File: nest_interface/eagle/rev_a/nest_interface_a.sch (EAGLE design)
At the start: 98 parts, among them J1 MOLEX_MICRO_USB_B_047346, J10 CONN_BLOCK_2, J11 CONN_BLOCK_2, J12 CONN_BLOCK_2, J13 CONN_BLOCK_2, J14 CONN_BLOCK_2, J15 CONN_BLOCK_2, J16 CONN_BLOCK_2, J17 CONN_BLOCK_3, J2 CONN_BLOCK_2, J3 CONN_BLOCK_3, J4 PJ-036A-SMT, J5 CONN_BLOCK_3, J6 CONN_BLOCK_3, J7 CONN_BLOCK_2, J8 CONN_BLOCK_3, J9 CONN_BLOCK_3, U1 FT232RL, U2 EPIC-CORE_A, U3 MPC1825

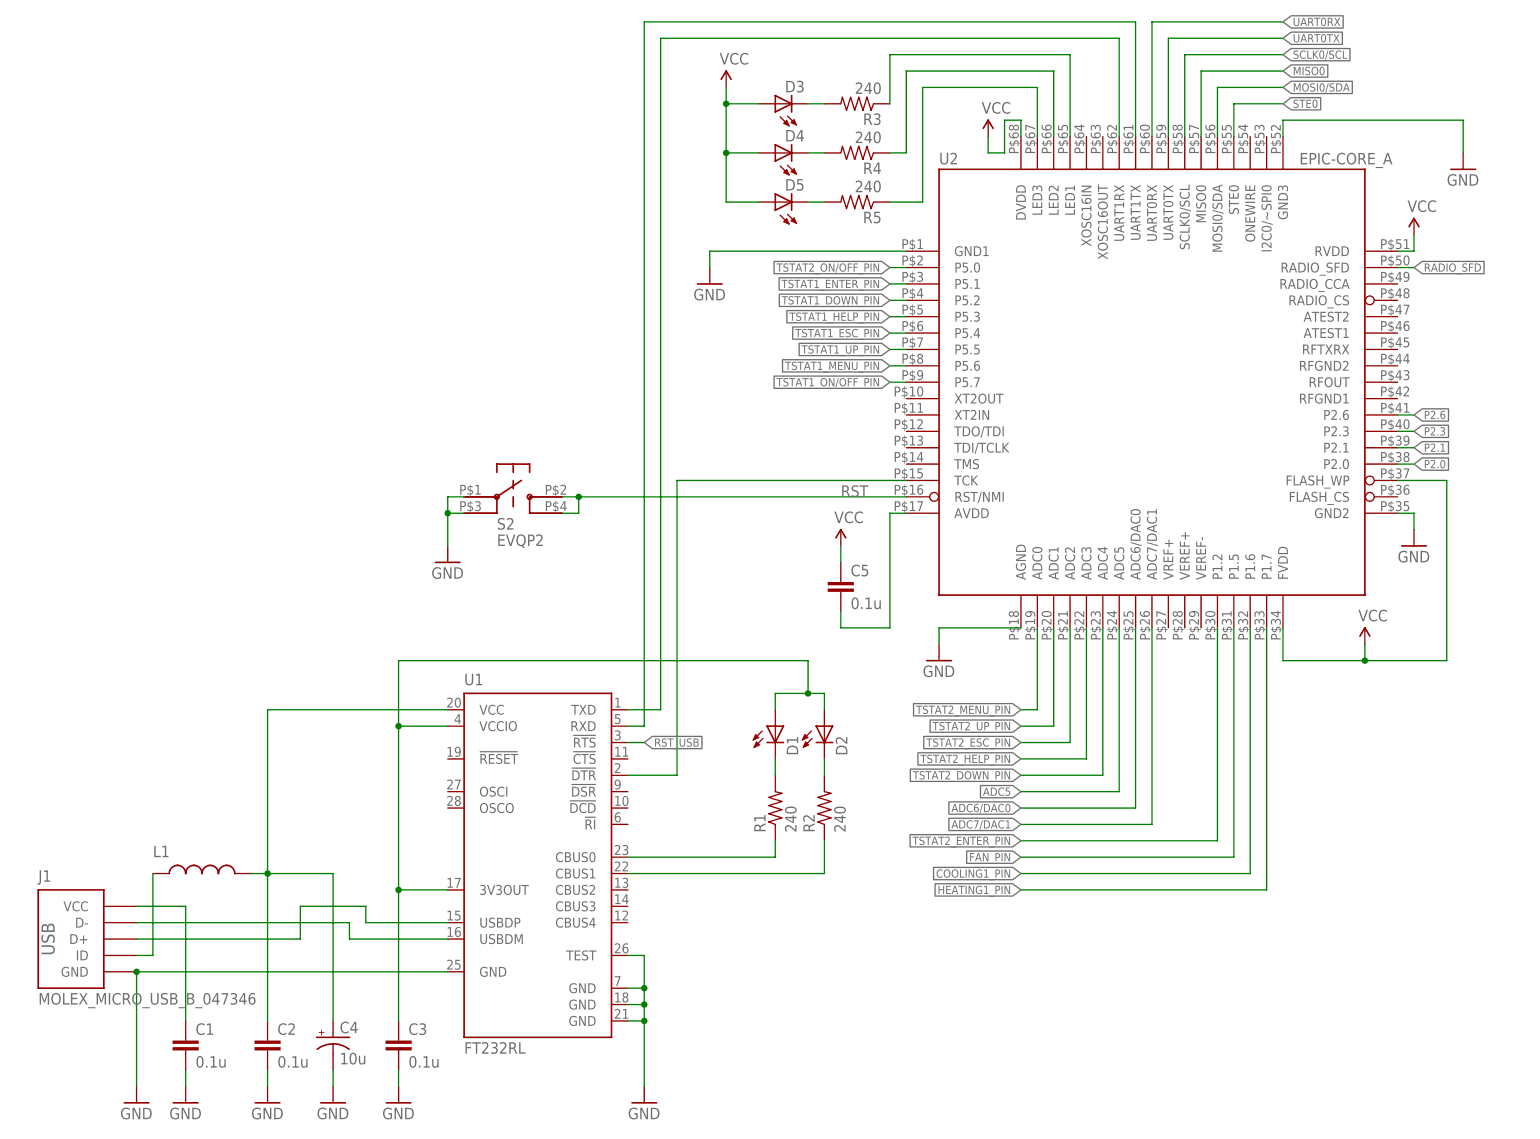
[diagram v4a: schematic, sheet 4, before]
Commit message: added relays
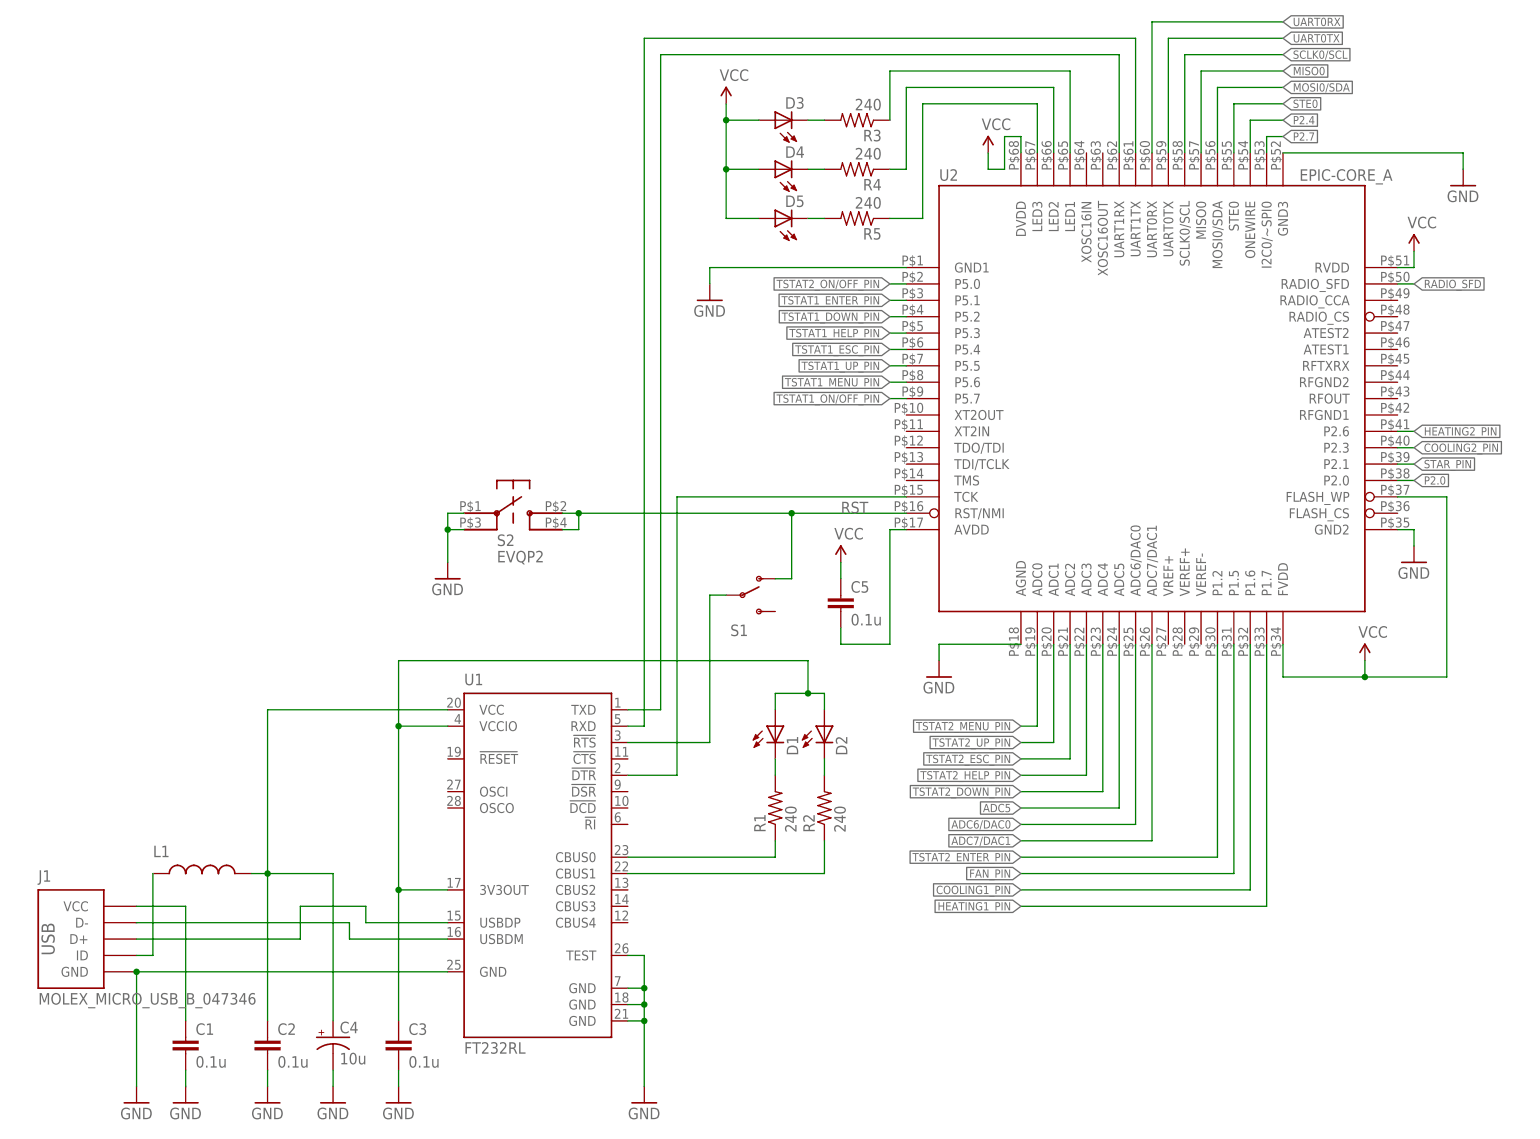
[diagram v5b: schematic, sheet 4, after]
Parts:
- removed J16: CONN_BLOCK_2, nest_interface:CONN_BLOCK_2
- added S1: (no value), SparkFun:SWITCH-SPSTPTH
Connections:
- removed net P2.1: JP1.3, U2.P2.1
- removed net P2.3: JP1.5, U2.P2.3
- removed net P2.6: JP1.7, U2.P2.6
- new net P2.4: JP1.5, U2.ONEWIRE
- new net P2.7: JP1.3, U2.I2C0/~SPI0
- net COOLING2_PIN: now also U2.P2.3
- net HEATING2_PIN: now also U2.P2.6
- net RST: now also S1.O; no longer J16.1
- net RST_USB: now also S1.P; no longer J16.2
- net STAR_PIN: now also U2.P2.1
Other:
- moved on the sheet: C5, D3, D4, D5, R3, R4, R5, S2, U2

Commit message: BETTER NEST
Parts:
- added R40, R41, R42, R43, R44, R45, R46, R47, R48, R49, R50, R51, R52, R53, R54, R55, R56, R57, R58, R59, R60, R61, R62, R63, R64, R65, R68, R69: 100k, rcl:R-US_R0603
- added R66, R67: 0, rcl:R-US_R0603
- added R70, R71: 10k, rcl:R-US_R0603
- added U$1, U$2, U$3, U$4: ALD1107, nest_interface:ALD1107
- added U4, U5: PCA9575, nest_interface:PCA9575
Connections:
- removed net TSTAT1_DOWN_PIN: R19.2, R20.1, U2.P5.2
- removed net TSTAT1_ENTER_PIN: R21.2, R22.1, U2.P5.1
- removed net TSTAT1_ESC_PIN: R15.2, R16.1, U2.P5.4
- removed net TSTAT1_HELP_PIN: R17.2, R18.1, U2.P5.3
- removed net TSTAT1_MENU_PIN: R11.2, R12.1, U2.P5.6
- removed net TSTAT1_ON/OFF_PIN: R10.1, R9.2, U2.P5.7
- removed net TSTAT1_UP_PIN: R13.2, R14.1, U2.P5.5
- removed net TSTAT2_DOWN_PIN: R33.2, R34.1, U2.ADC4
- removed net TSTAT2_ENTER_PIN: R35.2, R36.1, U2.P1.2
- removed net TSTAT2_ESC_PIN: R29.2, R30.1, U2.ADC2
- removed net TSTAT2_HELP_PIN: R31.2, R32.1, U2.ADC3
- removed net TSTAT2_MENU_PIN: R25.2, R26.1, U2.ADC0
- removed net TSTAT2_ON/OFF_PIN: R23.2, R24.1, U2.P5.0
- removed net TSTAT2_UP_PIN: R27.2, R28.1, U2.ADC1
- new net #KEYPAD_ENABLE: R40.2, R41.2, R42.2, R43.2, R48.2, R49.2, R50.2, R51.2, R56.2, R57.2, R58.2, R59.2, R64.2, R65.2, U$1.G1, U$1.G2, U$1.G3, U$1.G4, U$2.G1, U$2.G2, U$2.G3, U$2.G4, U$3.G1, U$3.G2, U$3.G3, U$3.G4, U$4.G1, U$4.G2
- new net I2C_SCL: R70.1, U2.SCLK0/SCL, U4.SCL, U5.SCL
- new net I2C_SDA: R71.1, U2.MOSI0/SDA, U4.SDA, U5.SDA
- new net N$37: R66.2, U4.#RESET
- new net N$58: R67.2, U5.#RESET
- new net TSTAT1_DOWN_IN: R53.1, U$2.S2, U4.P0_5
- new net TSTAT1_DOWN_OUT: Q6.C, U$2.D2
- new net TSTAT1_DOWN_OUT_PIN: R19.2, R20.1, U5.P0_5
- new net TSTAT1_ENTER_IN: R54.1, U$2.S3, U4.P0_6
- new net TSTAT1_ENTER_OUT: Q7.C, U$2.D3
- new net TSTAT1_ENTER_OUT_PIN: R21.2, R22.1, U5.P0_6
- new net TSTAT1_ESC_IN: R47.1, U$1.S4, U4.P0_3
- new net TSTAT1_ESC_OUT: Q4.C, U$1.D4
- new net TSTAT1_ESC_OUT_PIN: R15.2, R16.1, U5.P0_3
- new net TSTAT1_HELP_IN: R52.1, U$2.S1, U4.P0_4
- new net TSTAT1_HELP_OUT: Q5.C, U$2.D1
- new net TSTAT1_HELP_OUT_PIN: R17.2, R18.1, U5.P0_4
- new net TSTAT1_MENU_IN: R45.1, U$1.S2, U4.P0_1
- new net TSTAT1_MENU_OUT: Q2.C, U$1.D2
- new net TSTAT1_MENU_OUT_PIN: R11.2, R12.1, U5.P0_1
- new net TSTAT1_ON/OFF_IN: R44.1, U$1.S1, U4.P0_0
- new net TSTAT1_ON/OFF_OUT: Q1.C, U$1.D1
- new net TSTAT1_ON/OFF_OUT_PIN: R10.1, R9.2, U5.P0_0
- new net TSTAT1_UP_IN: R46.1, U$1.S3, U4.P0_2
- new net TSTAT1_UP_OUT: Q3.C, U$1.D3
- new net TSTAT1_UP_OUT_PIN: R13.2, R14.1, U5.P0_2
- new net TSTAT2_DOWN_IN: R68.1, U$4.S1, U4.P1_5
- new net TSTAT2_DOWN_OUT: Q13.C, U$4.D1
- new net TSTAT2_DOWN_OUT_PIN: R33.2, R34.1, U5.P1_5
- new net TSTAT2_ENTER_IN: R69.1, U$4.S2, U4.P1_6
- new net TSTAT2_ENTER_OUT: Q14.C, U$4.D2
- new net TSTAT2_ENTER_OUT_PIN: R35.2, R36.1, U5.P1_6
- new net TSTAT2_ESC_IN: R62.1, U$3.S3, U4.P1_3
- new net TSTAT2_ESC_OUT: Q11.C, U$3.D3
- new net TSTAT2_ESC_OUT_PIN: R29.2, R30.1, U5.P1_3
- new net TSTAT2_HELP_IN: R63.1, U$3.S4, U4.P1_4
- new net TSTAT2_HELP_OUT: Q12.C, U$3.D4
- new net TSTAT2_HELP_OUT_PIN: R31.2, R32.1, U5.P1_4
- new net TSTAT2_MENU_IN: R60.1, U$3.S1, U4.P1_1
- new net TSTAT2_MENU_OUT: Q9.C, U$3.D1
- new net TSTAT2_MENU_OUT_PIN: R25.2, R26.1, U5.P1_1
- new net TSTAT2_ON/OFF_IN: R55.1, U$2.S4, U4.P1_0
- new net TSTAT2_ON/OFF_OUT: Q8.C, U$2.D4
- new net TSTAT2_ON/OFF_OUT_PIN: R23.2, R24.1, U5.P1_0
- new net TSTAT2_UP_IN: R61.1, U$3.S2, U4.P1_2
- new net TSTAT2_UP_OUT: Q10.C, U$3.D2
- new net TSTAT2_UP_OUT_PIN: R27.2, R28.1, U5.P1_2
- new net TSTAT_IN_I2C_INT: U4.#INT
- new net TSTAT_OUT_I2C_INT: U5.#INT
- net GND: now also R40.1, R41.1, R42.1, R43.1, R48.1, R49.1, R50.1, R51.1, R56.1, R57.1, R58.1, R59.1, R64.1, R65.1, U$1.GND, U$2.GND, U$3.GND, U$4.GND, U4.ADDR3, U4.GND, U4.P0_7, U4.P1_7, U5.ADDR2, U5.ADDR3, U5.GND, U5.P0_7, U5.P1_7
- net MOSI0/SDA: no longer U2.MOSI0/SDA
- net SCLK0/SCL: no longer U2.SCLK0/SCL
- net TSTAT1_DOWN: no longer Q6.C
- net TSTAT1_ENTER: no longer Q7.C
- net TSTAT1_ESC: no longer Q4.C
- net TSTAT1_HELP: no longer Q5.C
- net TSTAT1_MENU: no longer Q2.C
- net TSTAT1_ON/OFF: no longer Q1.C
- net TSTAT1_UP: no longer Q3.C
- net TSTAT2_DOWN: no longer Q13.C
- net TSTAT2_ENTER: no longer Q14.C
- net TSTAT2_ESC: no longer Q11.C
- net TSTAT2_HELP: no longer Q12.C
- net TSTAT2_MENU: no longer Q9.C
- net TSTAT2_ON/OFF: no longer Q8.C
- net TSTAT2_UP: no longer Q10.C
- net VCC: now also R44.2, R45.2, R46.2, R47.2, R52.2, R53.2, R54.2, R55.2, R60.2, R61.2, R62.2, R63.2, R66.1, R67.1, R68.2, R69.2, R70.2, R71.2, U$1.VCC, U$2.VCC, U$3.VCC, U$4.VCC, U4.ADDR0, U4.ADDR1, U4.ADDR2, U4.P0_VCC, U4.P1_VCC, U4.VCC, U5.ADDR0, U5.ADDR1, U5.P0_VCC, U5.P1_VCC, U5.VCC
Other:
- note added: "All of the buttons from the thermostats."
- note added: "GPIO INPUTS"
- note added: "GPIO OUTPUTS"
- note added: "Outputs to make the thermostat think a button is pressed."

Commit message: saving nest i board
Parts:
- added C12, C13, C14, C17: 0.1u, rcl:C-EUC0603
- added C15: 10u, SparkFun:CAP_POL1206
- added C16: 1u, rcl:C-EUC0603
- added D10, D6, D7, D8, D9: (no value), SparkFun:LED0603
- added J16, J19, J20, J21, J23, J24: CONN_BLOCK_3, nest_interface:CONN_BLOCK_3
- added J18, J22: CONN_BLOCK_2, nest_interface:CONN_BLOCK_2
- added J25: MOLEX_MICRO_USB_B_047346, nest_interface:MOLEX_MICRO_USB_B_047346
- added L2: (no value), SparkFun:INDUCTOR0603
- added R72, R77: 100k, rcl:R-US_R0603
- added R73, R74, R78, R79, R80: 240, rcl:R-US_R0603
- added R75: 5.1M, rcl:R-US_R0603
- added R76: 100k 0.1%, rcl:R-US_R0603
- added RA1, RA2, RA3, RA4: VSSR2403103, nest_interface:VSSR2403103
- added S3: EVQP2, berkeley-epic:EVQP2
- added S4: (no value), SparkFun:SWITCH-SPSTPTH
- added U$5: MSP430F1611IPM, hijack:MSP430F1611IPM
- added U6: FT232RL, ftdichip:FT232RL
- added Y1: FC-135_32.768KA-A3, berkeley-epic:FC-135_32.768KA-A3
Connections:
- removed net TSTAT_OUT_I2C_INT: U5.#INT
- new net N$13: D8.C, R78.2
- new net N$38: U$5.XIN, Y1.1
- new net N$39: C12.1, J25.VCC
- new net N$40: J25.D-, U6.USBDM
- new net N$41: J25.D+, U6.USBDP
- new net N$42: J25.ID, L2.1
- new net N$43: C13.1, C15.+, L2.2, U6.VCC
- new net N$44: R73.1, U6.CBUS0
- new net N$45: R74.1, U6.CBUS1
- new net N$46: D6.C, R73.2
- new net N$47: D7.C, R74.2
- new net N$48: U$5.P3.6/UTXD1, U6.TXD
- new net N$49: U6.RXD
- new net N$50: U$5.TCK, U6.!DTR
- new net N$51: C14.1, D6.A, D7.A, U6.3V3OUT, U6.VCCIO
- new net N$52: R75.2, U$5.XOUT, Y1.2
- new net N$53: D9.C, R79.2
- new net N$54: R76.2, U$5.P2.5/ROSC
- new net N$55: D10.C, R80.2
- new net N$56: R79.1, U$5.P2.1/TAINCLK
- new net N$57: R80.1, U$5.P2.2/CAOUT/TA0/BSLRX
- new net N$8: R78.1, U$5.P2.0/ACLK
- new net RST1: C17.1, R77.2, S3.P$2, S3.P$4, S4.O, U$5.RST/NMI
- new net RST_USB1: S4.P, U6.!RTS
- new net TSTAT1_LCD_DB0: J19.1, RA1.7
- new net TSTAT1_LCD_DB0_PIN: RA1.17, RA1.18, U$5.P4.0/TB0
- new net TSTAT1_LCD_DB1: J19.2, RA1.9
- new net TSTAT1_LCD_DB1_PIN: RA1.15, RA1.16, U$5.P4.1/TB1
- new net TSTAT1_LCD_DB2: J19.3, RA1.11
- new net TSTAT1_LCD_DB2_PIN: RA1.13, RA1.14, U$5.P4.2/TB2
- new net TSTAT1_LCD_DB3: J20.1, RA2.1
- new net TSTAT1_LCD_DB3_PIN: RA2.23, RA2.24, U$5.P4.3/TB3
- new net TSTAT1_LCD_DB4: J20.2, RA2.3
- new net TSTAT1_LCD_DB4_PIN: RA2.21, RA2.22, U$5.P4.4/TB4
- new net TSTAT1_LCD_DB5: J20.3, RA2.5
- new net TSTAT1_LCD_DB5_PIN: RA2.19, RA2.20, U$5.P4.5/TB5
- new net TSTAT1_LCD_DB6: J18.1, RA2.7
- new net TSTAT1_LCD_DB6_PIN: RA2.17, RA2.18, U$5.P4.6/TB6
- new net TSTAT1_LCD_DB7: J18.2, RA2.9
- new net TSTAT1_LCD_DB7_PIN: RA2.15, RA2.16, U$5.P4.7/TBCLK
- new net TSTAT1_LCD_E: J16.3, RA1.5
- new net TSTAT1_LCD_E_PIN: RA1.19, RA1.20, U$5.P1.2/TA1
- new net TSTAT1_LCD_R/W: J16.2, RA1.3
- new net TSTAT1_LCD_R/W_PIN: RA1.21, RA1.22, U$5.P1.1/TA0/BSLTX
- new net TSTAT1_LCD_RS: J16.1, RA1.1
- new net TSTAT1_LCD_RS_PIN: RA1.23, RA1.24, U$5.P1.0/TACLK
- new net TSTAT2_LCD_DB0: J23.1, RA3.7
- new net TSTAT2_LCD_DB0_PIN: RA3.17, RA3.18, U$5.P6.0/A0
- new net TSTAT2_LCD_DB1: J23.2, RA3.9
- new net TSTAT2_LCD_DB1_PIN: RA3.15, RA3.16, U$5.P6.1/A1
- new net TSTAT2_LCD_DB2: J23.3, RA3.11
- new net TSTAT2_LCD_DB2_PIN: RA3.13, RA3.14, U$5.P6.2/A2
- new net TSTAT2_LCD_DB3: J24.1, RA4.1
- new net TSTAT2_LCD_DB3_PIN: RA4.23, RA4.24, U$5.P6.3/A3
- new net TSTAT2_LCD_DB4: J24.2, RA4.3
- new net TSTAT2_LCD_DB4_PIN: RA4.21, RA4.22, U$5.P6.4/A4
- new net TSTAT2_LCD_DB5: J24.3, RA4.5
- new net TSTAT2_LCD_DB5_PIN: RA4.19, RA4.20, U$5.P6.5/A5
- new net TSTAT2_LCD_DB6: J22.1, RA4.7
- new net TSTAT2_LCD_DB6_PIN: RA4.17, RA4.18, U$5.P6.6/A6/DAC0
- new net TSTAT2_LCD_DB7: J22.2, RA4.9
- new net TSTAT2_LCD_DB7_PIN: RA4.15, RA4.16, U$5.P6.7/A7/DAC1/SVSIN
- new net TSTAT2_LCD_E: J21.3, RA3.5
- new net TSTAT2_LCD_E_PIN: RA3.19, RA3.20, U$5.P1.5/TA0
- new net TSTAT2_LCD_R/W: J21.2, RA3.3
- new net TSTAT2_LCD_R/W_PIN: RA3.21, RA3.22, U$5.P1.4/SMCLK
- new net TSTAT2_LCD_RS: J21.1, RA3.1
- new net TSTAT2_LCD_RS_PIN: RA3.23, RA3.24, U$5.P1.3/TA2
- net GND: now also C12.2, C13.2, C14.2, C15.-, C16.2, C17.2, J25.GND, R75.1, RA1.10, RA1.12, RA1.2, RA1.4, RA1.6, RA1.8, RA2.10, RA2.2, RA2.4, RA2.6, RA2.8, RA3.10, RA3.12, RA3.2, RA3.4, RA3.6, RA3.8, RA4.10, RA4.2, RA4.4, RA4.6, RA4.8, S3.P$1, S3.P$3, U$5.AVSS, U$5.DVSS1, U$5.VEREF+, U$5.VREF-/VEREF-, U$5.XT2IN, U6.GND, U6.GND@1, U6.GND@2, U6.GND@A, U6.TEST; no longer U5.P0_7, U5.P1_7
- net I2C_SCL: now also U$5.P3.3/UCLK0/SCL
- net I2C_SDA: now also U$5.P3.1/MOSI0/SDA
- net TSTAT_IN_I2C_INT: now also R72.2
- net VCC: now also C16.1, D10.A, D8.A, D9.A, R72.1, R76.1, R77.1, U$5.AVCC, U$5.DVCC

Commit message: started routing wow is that going to be tricky
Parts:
- removed J10, J18, J22: CONN_BLOCK_2, nest_interface:CONN_BLOCK_2
- removed J16, J19, J20, J21, J9: CONN_BLOCK_3, nest_interface:CONN_BLOCK_3
- removed Q1, Q10, Q11, Q12, Q13, Q14, Q2, Q3, Q4, Q5, Q6, Q7, Q8, Q9: (no value), nest_interface:TRANSISTOR_NPNSOT23-3
- removed R12, R14, R16, R18, R20, R22, R24, R26, R28, R30, R32, R34, R36, R40, R41, R42, R43, R44, R45, R46, R47, R48, R49, R50, R51, R52, R53, R54, R55, R56, R57, R58, R59, R60, R61, R62, R63, R64, R65, R68, R69: 100k, rcl:R-US_R0603
- removed R13, R15, R17, R19, R21, R23, R25, R27, R29, R31, R70, R71: 10k, rcl:R-US_R0603
- removed RA3: VSSR2403103, nest_interface:VSSR2403103
- removed U$1, U$2, U$3, U$4: ALD1107, nest_interface:ALD1107
- added J30: PINH2X12, SparkFun:PINH2X12
- added QA1, QA2, QA3, QA4: MMPQ2222A, nest_interface:MMPQ2222A
- added RA5, RA6: 766161104GP, nest_interface:766161104GP
- added RA7: VSSR1603103, nest_interface:VSSR1603103
- added U10, U11, U8, U9: ALD1107, nest_interface:ALD1107
- added U7: TC1262, nest_interface:TC1262
- J23, J24, J5, J6: value CONN_BLOCK_3 -> CONN_BLOCK_8; device nest_interface:CONN_BLOCK_3 -> nest_interface:CONN_BLOCK_8
- J7: value CONN_BLOCK_2 -> CONN_BLOCK_7; device nest_interface:CONN_BLOCK_2 -> nest_interface:CONN_BLOCK_7
- J8: value CONN_BLOCK_3 -> CONN_BLOCK_7; device nest_interface:CONN_BLOCK_3 -> nest_interface:CONN_BLOCK_7
- R10: value 100k -> 10k
- R66, R67: value 0 -> 100k
- R9: value 10k -> 100k
- renumbered U$5 to U20
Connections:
- net MISO0 renamed EPIC_MISO0
- net P2.0 renamed EPIC_P2.0
- net P2.4 renamed EPIC_P2.4
- net P2.7 renamed EPIC_P2.7
- net STE0 renamed EPIC_STE0
- net UART0RX renamed EPIC_UART0RX
- net UART0TX renamed EPIC_UART0TX
- removed net ADC5: JP1.16, U2.ADC5
- removed net ADC6/DAC0: JP1.14, U2.ADC6/DAC0
- removed net ADC7/DAC1: JP1.12, U2.ADC7/DAC1
- removed net MOSI0/SDA: JP1.11
- removed net N$16: Q2.B, R11.1
- removed net N$17: Q1.B, R9.1
- removed net N$25: Q3.B, R13.1
- removed net N$26: Q4.B, R15.1
- removed net N$27: Q5.B, R17.1
- removed net N$28: Q6.B, R19.1
- removed net N$29: Q7.B, R21.1
- removed net N$30: Q8.B, R23.1
- removed net N$31: Q9.B, R25.1
- removed net N$32: Q10.B, R27.1
- removed net N$33: Q11.B, R29.1
- removed net N$34: Q12.B, R31.1
- removed net N$42: J25.ID, L2.1
- removed net N$5: J1.ID, L1.1
- removed net SCLK0/SCL: JP1.15
- removed net TSTAT1_DOWN: J6.1
- removed net TSTAT1_ENTER: J7.2
- removed net TSTAT1_ESC: J6.3
- removed net TSTAT1_HELP: J6.2
- removed net TSTAT1_LCD_DB0: J19.1, RA1.7
- removed net TSTAT1_LCD_DB0_PIN: RA1.17, RA1.18, U20.P4.0/TB0
- removed net TSTAT1_LCD_DB1: J19.2, RA1.9
- removed net TSTAT1_LCD_DB1_PIN: RA1.15, RA1.16, U20.P4.1/TB1
- removed net TSTAT1_LCD_DB2: J19.3, RA1.11
- removed net TSTAT1_LCD_DB2_PIN: RA1.13, RA1.14, U20.P4.2/TB2
- removed net TSTAT1_LCD_DB3: J20.1, RA2.1
- removed net TSTAT1_LCD_DB3_PIN: RA2.23, RA2.24, U20.P4.3/TB3
- removed net TSTAT1_MENU: J5.2
- removed net TSTAT1_ON/OFF: J5.3
- removed net TSTAT1_UP: J5.1
- removed net TSTAT2_DOWN: J9.1
- removed net TSTAT2_ENTER: J10.2
- removed net TSTAT2_ESC: J9.3
- removed net TSTAT2_HELP: J9.2
- removed net TSTAT2_LCD_DB0: J23.1, RA3.7
- removed net TSTAT2_LCD_DB0_PIN: RA3.17, RA3.18, U20.P6.0/A0
- removed net TSTAT2_LCD_DB1: J23.2, RA3.9
- removed net TSTAT2_LCD_DB1_PIN: RA3.15, RA3.16, U20.P6.1/A1
- removed net TSTAT2_LCD_DB2: J23.3, RA3.11
- removed net TSTAT2_LCD_DB2_PIN: RA3.13, RA3.14, U20.P6.2/A2
- removed net TSTAT2_LCD_DB3: J24.1, RA4.1
- removed net TSTAT2_LCD_DB3_PIN: RA4.23, RA4.24, U20.P6.3/A3
- removed net TSTAT2_MENU: J8.2
- removed net TSTAT2_ON/OFF: J8.3
- removed net TSTAT2_UP: J8.1
- new net 5.6V_SUPPLY: J11.2, U3.VIN, U7.VIN
- new net EPIC_ADC1: JP1.18, U2.ADC1
- new net EPIC_ADC2: JP1.16, U2.ADC2
- new net EPIC_ADC3: JP1.14, U2.ADC3
- new net EPIC_ADC4: JP1.12, U2.ADC4
- new net EPIC_ADC5: JP1.10, U2.ADC5
- new net EPIC_ADC6/DAC0: JP1.8, U2.ADC6/DAC0
- new net EPIC_ADC7/DAC1: JP1.6, U2.ADC7/DAC1
- new net EPIC_P5.7: JP1.7, U2.P5.7
- new net LCDP_MISO0: J30.16, U20.P3.2/MISO0
- new net LCDP_P2.4: J30.4, U20.P2.4/CA1/TA2
- new net LCDP_P2.7: U20.P2.7/TA0
- new net LCDP_STE0: J30.18, U20.P3.0/STE0
- new net LCDP_URXD0: J30.12, U20.P3.5/URXD0
- new net LCDP_UTXD0: J30.14, U20.P3.4/UTXD0
- new net N$59: QA1.B3, RA4.22
- new net N$60: QA1.B4, RA4.21
- new net N$61: QA2.B1, RA4.20
- new net N$62: QA2.B2, RA4.19
- new net N$63: QA2.B3, RA4.18
- new net N$64: QA2.B4, RA4.17
- new net N$65: QA3.B1, RA4.16
- new net N$66: QA3.B2, RA4.15
- new net N$67: QA3.B3, RA4.14
- new net N$68: QA3.B4, RA4.13
- new net P1.6: J30.10, U20.P1.6/TA1
- new net P1.7: J30.8, U20.P1.7/TA2
- new net P2.3: J30.6, U20.P2.3/CA0/TA1
- new net P2.6: J30.2, U20.P2.6/ADC12CLK/DMAE0
- new net P5.0: J30.1, U20.P5.0/STE1
- new net P5.1: J30.3, U20.P5.1/MOSI1
- new net P5.2: J30.5, U20.P5.2/MISO1
- new net P5.3: J30.7, U20.P5.3/UCLK1
- new net P5.4: J30.9, U20.P5.4/MCLK
- new net P5.5: U20.P5.5/SMCLK
- new net P5.6: J30.11, U20.P5.6/ACLK
- new net P5.7: J30.13, U20.P5.7/TBOUTH/SVSOUT
- new net P6.0: J30.15, U20.P6.0/A0
- new net P6.1: J30.17, U20.P6.1/A1
- new net P6.2: J30.19, U20.P6.2/A2
- new net P6.3: J30.21, U20.P6.3/A3
- new net P6.4: J30.23, U20.P6.4/A4
- new net P6.5: J30.24, U20.P6.5/A5
- new net P6.6: J30.22, U20.P6.6/A6/DAC0
- new net P6.7: J30.20, U20.P6.7/A7/DAC1/SVSIN
- new net TSTAT_IN_I2C_RST: R66.2, U2.P5.0, U4.#RESET
- new net TSTAT_OUT_I2C_RST: R67.2, U2.P5.1, U5.#RESET
- net #KEYPAD_ENABLE: now also R9.1, U10.G1, U10.G2, U10.G3, U10.G4, U11.G1, U11.G2, U2.P5.2, U8.G1, U8.G2, U8.G3, U8.G4, U9.G1, U9.G2, U9.G3, U9.G4; no longer R40.2, R41.2, R42.2, R43.2, R48.2, R49.2, R50.2, R51.2, R56.2, R57.2, R58.2, R59.2, R64.2, R65.2, U$1.G1, U$1.G2, U$1.G3, U$1.G4, U$2.G1, U$2.G2, U$2.G3, U$2.G4, U$3.G1, U$3.G2, U$3.G3, U$3.G4, U$4.G1, U$4.G2
- net 5V: now also U7.VOUT; no longer J11.2, U3.VIN
- net GND: now also J23.1, J24.1, J5.1, J6.1, QA1.E1, QA1.E2, QA1.E3, QA1.E4, QA2.E1, QA2.E2, QA2.E3, QA2.E4, QA3.E1, QA3.E2, QA3.E3, QA3.E4, QA4.E1, QA4.E2, R9.2, RA2.12, RA5.OUT, RA7.2, RA7.4, U10.GND, U11.GND, U7.GND, U8.GND, U9.GND; no longer J10.1, J7.1, Q1.E, Q10.E, Q11.E, Q12.E, Q13.E, Q14.E, Q2.E, Q3.E, Q4.E, Q5.E, Q6.E, Q7.E, Q8.E, Q9.E, R10.2, R12.2, R14.2, R16.2, R18.2, R20.2, R22.2, R24.2, R26.2, R28.2, R30.2, R32.2, R34.2, R36.2, R40.1, R41.1, R42.1, R43.1, R48.1, R49.1, R50.1, R51.1, R56.1, R57.1, R58.1, R59.1, R64.1, R65.1, RA3.10, RA3.12, RA3.2, RA3.4, RA3.6, RA3.8, RA4.10, RA4.2, RA4.4, RA4.6, RA4.8, U$1.GND, U$2.GND, U$3.GND, U$4.GND
- net I2C_SCL: now also JP1.15, R10.2; no longer R70.1
- net I2C_SDA: now also JP1.11, R11.2; no longer R71.1
- net N$1: now also L1.1
- net N$35: no longer Q13.B
- net N$36: no longer Q14.B
- net N$37: now also QA1.B1, RA4.24; no longer R66.2, U4.#RESET
- net N$39: now also L2.1
- net N$49: now also U20.P3.7/URXD1
- net N$58: now also QA1.B2, RA4.23; no longer R67.2, U5.#RESET
- net RADIO_SFD: now also JP1.4; no longer JP1.10
- net TSTAT1_DOWN_IN: now also J5.3, RA6.6, U4.P0_1, U9.S2; no longer R53.1, U$2.S2, U4.P0_5
- net TSTAT1_DOWN_OUT: now also J23.3, QA2.C2, U9.D2; no longer Q6.C, U$2.D2
- net TSTAT1_DOWN_OUT_PIN: now also RA4.6, RA5.3; no longer R19.2, R20.1
- net TSTAT1_ENTER_IN: now also J5.2, RA6.7, U4.P0_0, U9.S3; no longer R54.1, U$2.S3, U4.P0_6
- net TSTAT1_ENTER_OUT: now also J23.2, QA2.C3, U9.D3; no longer Q7.C, U$2.D3
- net TSTAT1_ENTER_OUT_PIN: now also RA4.7, RA5.2; no longer R21.2, R22.1
- net TSTAT1_ESC_IN: now also J5.5, RA6.4, U8.S4; no longer R47.1, U$1.S4
- net TSTAT1_ESC_OUT: now also J23.5, QA1.C4, U8.D4; no longer Q4.C, U$1.D4
- net TSTAT1_ESC_OUT_PIN: now also RA4.4, RA5.5; no longer R15.2, R16.1
- net TSTAT1_HELP_IN: now also J5.4, RA6.5, U4.P0_2, U9.S1; no longer R52.1, U$2.S1, U4.P0_4
- net TSTAT1_HELP_OUT: now also J23.4, QA2.C1, U9.D1; no longer Q5.C, U$2.D1
- net TSTAT1_HELP_OUT_PIN: now also RA4.5, RA5.4; no longer R17.2, R18.1
- net TSTAT1_LCD_DB4: now also J7.4, RA1.7; no longer J20.2, RA2.3
- net TSTAT1_LCD_DB4_PIN: now also RA1.17, RA1.18, U20.P4.0/TB0; no longer RA2.21, RA2.22, U20.P4.4/TB4
- net TSTAT1_LCD_DB5: now also J7.5, RA1.9; no longer J20.3, RA2.5
- net TSTAT1_LCD_DB5_PIN: now also RA1.15, RA1.16, U20.P4.1/TB1; no longer RA2.19, RA2.20, U20.P4.5/TB5
- net TSTAT1_LCD_DB6: now also J7.6, RA1.11; no longer J18.1, RA2.7
- net TSTAT1_LCD_DB6_PIN: now also RA1.13, RA1.14, U20.P4.2/TB2; no longer RA2.17, RA2.18, U20.P4.6/TB6
- net TSTAT1_LCD_DB7: now also J7.7, RA2.1; no longer J18.2, RA2.9
- net TSTAT1_LCD_DB7_PIN: now also RA2.23, RA2.24, U20.P4.3/TB3; no longer RA2.15, RA2.16, U20.P4.7/TBCLK
- net TSTAT1_LCD_E: now also J7.3; no longer J16.3
- net TSTAT1_LCD_E_PIN: now also U20.P1.3/TA2; no longer U20.P1.2/TA1
- net TSTAT1_LCD_R/W: now also J7.2; no longer J16.2
- net TSTAT1_LCD_R/W_PIN: now also U20.P1.4/SMCLK; no longer U20.P1.1/TA0/BSLTX
- net TSTAT1_LCD_RS: now also J7.1; no longer J16.1
- net TSTAT1_LCD_RS_PIN: now also U20.P1.5/TA0; no longer U20.P1.0/TACLK
- net TSTAT1_MENU_IN: now also J5.7, RA6.2, U4.P0_5, U8.S2; no longer R45.1, U$1.S2, U4.P0_1
- net TSTAT1_MENU_OUT: now also J23.7, QA1.C2, U8.D2; no longer Q2.C, U$1.D2
- net TSTAT1_MENU_OUT_PIN: now also RA4.2, RA5.7; no longer R11.2, R12.1
- net TSTAT1_ON/OFF_IN: now also J5.8, RA6.1, U4.P0_6, U8.S1; no longer R44.1, U$1.S1, U4.P0_0
- net TSTAT1_ON/OFF_OUT: now also J23.8, QA1.C1, U8.D1; no longer Q1.C, U$1.D1
- net TSTAT1_ON/OFF_OUT_PIN: now also RA4.1, RA5.8; no longer R10.1, R9.2
- net TSTAT1_UP_IN: now also J5.6, RA6.3, U4.P0_4, U8.S3; no longer R46.1, U$1.S3, U4.P0_2
- net TSTAT1_UP_OUT: now also J23.6, QA1.C3, U8.D3; no longer Q3.C, U$1.D3
- net TSTAT1_UP_OUT_PIN: now also RA4.3, RA5.6; no longer R13.2, R14.1
- net TSTAT2_DOWN_IN: now also J6.3, RA6.13, U11.S1; no longer R68.1, U$4.S1
- net TSTAT2_DOWN_OUT: now also J24.3, QA4.C1, U11.D1; no longer Q13.C, U$4.D1
- net TSTAT2_DOWN_OUT_PIN: now also RA5.13; no longer R34.1
- net TSTAT2_ENTER_IN: now also J6.2, RA6.14, U11.S2; no longer R69.1, U$4.S2
- net TSTAT2_ENTER_OUT: now also J24.2, QA4.C2, U11.D2; no longer Q14.C, U$4.D2
- net TSTAT2_ENTER_OUT_PIN: now also RA5.14; no longer R36.1
- net TSTAT2_ESC_IN: now also J6.5, RA6.11, U10.S3; no longer R62.1, U$3.S3
- net TSTAT2_ESC_OUT: now also J24.5, QA3.C3, U10.D3; no longer Q11.C, U$3.D3
- net TSTAT2_ESC_OUT_PIN: now also RA4.11, RA5.10; no longer R29.2, R30.1
- net TSTAT2_HELP_IN: now also J6.4, RA6.12, U10.S4; no longer R63.1, U$3.S4
- net TSTAT2_HELP_OUT: now also J24.4, QA3.C4, U10.D4; no longer Q12.C, U$3.D4
- net TSTAT2_HELP_OUT_PIN: now also RA4.12, RA5.9; no longer R31.2, R32.1
- net TSTAT2_LCD_DB4: now also J8.4, RA2.9; no longer J24.2, RA4.3
- net TSTAT2_LCD_DB4_PIN: now also RA2.15, RA2.16, U20.P4.4/TB4; no longer RA4.21, RA4.22, U20.P6.4/A4
- net TSTAT2_LCD_DB5: now also J8.5, RA2.11; no longer J24.3, RA4.5
- net TSTAT2_LCD_DB5_PIN: now also RA2.13, RA2.14, U20.P4.5/TB5; no longer RA4.19, RA4.20, U20.P6.5/A5
- net TSTAT2_LCD_DB6: now also J8.6, RA7.1; no longer J22.1, RA4.7
- net TSTAT2_LCD_DB6_PIN: now also RA7.15, RA7.16, U20.P4.6/TB6; no longer RA4.17, RA4.18, U20.P6.6/A6/DAC0
- net TSTAT2_LCD_DB7: now also J8.7, RA7.3; no longer J22.2, RA4.9
- net TSTAT2_LCD_DB7_PIN: now also RA7.13, RA7.14, U20.P4.7/TBCLK; no longer RA4.15, RA4.16, U20.P6.7/A7/DAC1/SVSIN
- net TSTAT2_LCD_E: now also J8.3, RA2.7; no longer J21.3, RA3.5
- net TSTAT2_LCD_E_PIN: now also RA2.17, RA2.18, U20.P1.2/TA1; no longer RA3.19, RA3.20, U20.P1.5/TA0
- net TSTAT2_LCD_R/W: now also J8.2, RA2.5; no longer J21.2, RA3.3
- net TSTAT2_LCD_R/W_PIN: now also RA2.19, RA2.20, U20.P1.1/TA0/BSLTX; no longer RA3.21, RA3.22, U20.P1.4/SMCLK
- net TSTAT2_LCD_RS: now also J8.1, RA2.3; no longer J21.1, RA3.1
- net TSTAT2_LCD_RS_PIN: now also RA2.21, RA2.22, U20.P1.0/TACLK; no longer RA3.23, RA3.24, U20.P1.3/TA2
- net TSTAT2_MENU_IN: now also J6.7, RA6.9, U10.S1; no longer R60.1, U$3.S1
- net TSTAT2_MENU_OUT: now also J24.7, QA3.C1, U10.D1; no longer Q9.C, U$3.D1
- net TSTAT2_MENU_OUT_PIN: now also RA4.9, RA5.12; no longer R25.2, R26.1
- net TSTAT2_ON/OFF_IN: now also J6.8, RA6.8, U9.S4; no longer R55.1, U$2.S4
- net TSTAT2_ON/OFF_OUT: now also J24.8, QA2.C4, U9.D4; no longer Q8.C, U$2.D4
- net TSTAT2_ON/OFF_OUT_PIN: now also RA4.8, RA5.1; no longer R23.2, R24.1
- net TSTAT2_UP_IN: now also J6.6, RA6.10, U10.S2; no longer R61.1, U$3.S2
- net TSTAT2_UP_OUT: now also J24.6, QA3.C2, U10.D2; no longer Q10.C, U$3.D2
- net TSTAT2_UP_OUT_PIN: now also RA4.10, RA5.11; no longer R27.2, R28.1
- net TSTAT_IN_I2C_INT: now also U2.P1.2
- net VCC: now also R10.1, R11.1, RA6.OUT, U10.VCC, U11.VCC, U8.VCC, U9.VCC; no longer R44.2, R45.2, R46.2, R47.2, R52.2, R53.2, R54.2, R55.2, R60.2, R61.2, R62.2, R63.2, R68.2, R69.2, R70.2, R71.2, U$1.VCC, U$2.VCC, U$3.VCC, U$4.VCC
